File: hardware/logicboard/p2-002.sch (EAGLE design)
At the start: 18 parts, among them IC1 74LS07N, U1 DS18B20

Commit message: Writing.
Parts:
- removed H1, H2: STAND-OFF, SparkFun-Hardware:STAND-OFF
- removed JP2: RTC, SparkFun-Connectors:CONN_05
- added J0: (no value), con-jack:JACK-PLUG0
- added J1, J2: DIN5, SparkFun-Connectors:DIN5
- added SV1: (no value), con-ml:ML10LE
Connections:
- removed net V+: JP5.3
- net GND: now also J0.1, J0.2, J2.2; no longer JP2.2
- net MIRTN: now also J1.5
- net MISND: now also J1.4
- net MTRTN: now also J2.5
- net MTSND: now also J2.4
- net SCL: no longer JP2.4
- net SDA: no longer JP2.5
- net VCC: no longer JP2.1
- net VIN: now also J0.3, JP5.3

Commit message: Wiring.
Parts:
- removed C6, C7: 10n, resistor:C-EU025-024X044
- RN3: value 220 -> (none)
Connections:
- new net N$1: IC1B.O, RN3E.1
- new net N$2: IC1C.O, RN3G.1
- net GND: now also SV1-8.S; no longer C6.2, C7.2
- net GPIO1: now also SV1-1.S
- net GPIO2: now also SV1-7.S
- net MISO: now also SV1-3.S
- net MOSI: now also SV1-6.S
- net RX: now also IC1B.I, IC1C.I
- net SCK: now also SV1-5.S
- net VCC: now also RN3D.1, RN3F.1, SV1-4.S; no longer C6.1, C7.1
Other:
- moved on the sheet: D3, IC1A, IC1B, IC1C, OK1, RN3A, RN3B, RN3C, RN3E, RN3F, RN3G

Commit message: First working version of MIDI IN, MIDI THRU, SPI edition.
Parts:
- added JD1: DIN5, SparkFun-Connectors:DIN5
- added SV4: (no value), con-ml:ML14E
- added SV5: (no value), con-ml:ML10E
- J1: value DIN5 -> (none); device SparkFun-Connectors:DIN5 -> SparkFun-Connectors:CONN_05JST
- renumbered J2 to JD2, SV1 to SV3
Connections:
- net N$1 renamed MO
- net N$2 renamed MO2
- new net MO2RTN: RN3G.2, SV5-10.S
- new net MO2SND: RN3F.2, SV5-9.S
- new net MORTN: RN3E.2, SV5-8.S
- new net MOSND: RN3D.2, SV5-7.S
- net ANLG1: now also SV4-8.S
- net ANLG2: now also SV4-9.S
- net ANLG3: now also SV4-10.S
- net ANLG4: now also SV4-11.S
- net D7: now also J1.4
- net DTCT1: now also SV4-4.S
- net DTCT2: now also SV4-5.S
- net DTCT3: now also SV4-6.S
- net DTCT4: now also SV4-7.S
- net GATE: now also SV4-12.S
- net GND: now also J1.1, SV4-1.S, SV5-3.S, SV5-6.S
- net LED0: now also SV4-13.S
- net LED1: now also SV4-14.S
- net MIRTN: now also JD1.5, SV5-2.S; no longer J1.5
- net MISND: now also JD1.4, SV5-1.S; no longer J1.4
- net MTRTN: now also SV5-5.S
- net MTSND: now also SV5-4.S
- net RLY: now also SV4-3.S
- net RX: no longer IC1B.I, IC1C.I
- net SCL: now also J1.3
- net SDA: now also J1.2
- net TX: now also IC1B.I, IC1C.I
- net VCC: now also J1.5, SV4-2.S

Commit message: DIP SW.
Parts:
- added S1, S2: (no value), switch-dil:A1353HEX
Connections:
- net ANLG1: now also S2.1
- net ANLG2: now also S2.2
- net ANLG3: now also S2.4
- net ANLG4: now also S2.8
- net DTCT1: now also S1.1
- net DTCT2: now also S1.2
- net DTCT3: now also S1.4
- net DTCT4: now also S1.8
- net GND: now also S1.C, S2.C
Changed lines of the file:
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@@
 <part name="J1" library="SparkFun-Connectors" library_urn="urn:adsk.eagle:library:513" deviceset="CONN_05" device="JST" package3d_urn="urn:adsk.eagle:package:38120/1"/>
 <part name="SV5" library="con-ml" library_urn="urn:adsk.eagle:library:164" deviceset="ML10E" device="" package3d_urn="urn:adsk.eagle:package:8676/1"/>
+<part name="S1" library="switch-dil" library_urn="urn:adsk.eagle:library:375" deviceset="A1353HEX" device="" package3d_urn="urn:adsk.eagle:package:27207/1"/>
+<part name="S2" library="switch-dil" library_urn="urn:adsk.eagle:library:375" deviceset="A1353HEX" device="" package3d_urn="urn:adsk.eagle:package:27207/1"/>
 </parts>
 <sheets>
@@
 <attribute name="VALUE" x="68.834" y="83.439" size="1.778" layer="96" rot="MR0"/>
 </instance>
+<instance part="S1" gate="1" x="241.3" y="63.5" smashed="yes" rot="R270">
+<attribute name="NAME" x="236.22" y="67.945" size="1.778" layer="95"/>
+<attribute name="VALUE" x="236.22" y="54.61" size="1.778" layer="96"/>
+</instance>
+<instance part="S2" gate="1" x="241.3" y="48.26" smashed="yes" rot="R270">
+<attribute name="NAME" x="236.22" y="52.705" size="1.778" layer="95"/>
+<attribute name="VALUE" x="236.22" y="39.37" size="1.778" layer="96"/>
+</instance>
 </instances>
 <busses>
@@
 <label x="73.66" y="106.68" size="0.8128" layer="95" xref="yes"/>
 </segment>
+<segment>
+<pinref part="S1" gate="1" pin="C"/>
+<wire x1="233.68" y1="63.5" x2="231.14" y2="63.5" width="0.1524" layer="91"/>
+<label x="231.14" y="63.5" size="0.8128" layer="95" rot="R180" xref="yes"/>
+</segment>
+<segment>
+<pinref part="S2" gate="1" pin="C"/>
+<wire x1="233.68" y1="48.26" x2="231.14" y2="48.26" width="0.1524" layer="91"/>
+<label x="231.14" y="48.26" size="0.8128" layer="95" rot="R180" xref="yes"/>
+</segment>
 </net>
 <net name="VCC" class="2">
@@
 <label x="187.96" y="48.26" size="0.8128" layer="95" xref="yes"/>
 </segment>
+<segment>
+<pinref part="S2" gate="1" pin="8"/>
+<wire x1="248.92" y1="43.18" x2="251.46" y2="43.18" width="0.1524" layer="91"/>
+<label x="251.46" y="43.18" size="0.8128" layer="95" xref="yes"/>
+</segment>
 </net>
 <net name="ANLG3" class="0">
@@
 <label x="187.96" y="53.34" size="0.8128" layer="95" xref="yes"/>
 </segment>
+<segment>
+<pinref part="S2" gate="1" pin="4"/>
+<wire x1="248.92" y1="45.72" x2="251.46" y2="45.72" width="0.1524" layer="91"/>
+<label x="251.46" y="45.72" size="0.8128" layer="95" xref="yes"/>
+</segment>
 </net>
 <net name="ANLG2" class="0">
@@
 <label x="187.96" y="58.42" size="0.8128" layer="95" xref="yes"/>
 </segment>
+<segment>
+<pinref part="S2" gate="1" pin="2"/>
+<wire x1="248.92" y1="48.26" x2="251.46" y2="48.26" width="0.1524" layer="91"/>
+<label x="251.46" y="48.26" size="0.8128" layer="95" xref="yes"/>
+</segment>
 </net>
 <net name="ANLG1" class="0">
@@
 <wire x1="185.42" y1="63.5" x2="187.96" y2="63.5" width="0.1524" layer="91"/>
 <label x="187.96" y="63.5" size="0.8128" layer="95" xref="yes"/>
+</segment>
+<segment>
+<pinref part="S2" gate="1" pin="1"/>
+<wire x1="248.92" y1="50.8" x2="251.46" y2="50.8" width="0.1524" layer="91"/>
+<label x="251.46" y="50.8" size="0.8128" layer="95" xref="yes"/>
 </segment>
 </net>
@@
 <label x="152.4" y="48.26" size="0.8128" layer="95" xref="yes"/>
 </segment>
+<segment>
+<pinref part="S1" gate="1" pin="1"/>
+<wire x1="248.92" y1="66.04" x2="251.46" y2="66.04" width="0.1524" layer="91"/>
+<label x="251.46" y="66.04" size="0.8128" layer="95" xref="yes"/>
+</segment>
 </net>
 <net name="DTCT2" class="0">
@@
 <label x="152.4" y="43.18" size="0.8128" layer="95" xref="yes"/>
 </segment>
+<segment>
+<pinref part="S1" gate="1" pin="2"/>
+<wire x1="248.92" y1="63.5" x2="251.46" y2="63.5" width="0.1524" layer="91"/>
+<label x="251.46" y="63.5" size="0.8128" layer="95" xref="yes"/>
+</segment>
 </net>
 <net name="DTCT3" class="0">
@@
 <label x="152.4" y="38.1" size="0.8128" layer="95" xref="yes"/>
 </segment>
+<segment>
+<pinref part="S1" gate="1" pin="4"/>
+<wire x1="248.92" y1="60.96" x2="251.46" y2="60.96" width="0.1524" layer="91"/>
+<label x="251.46" y="60.96" size="0.8128" layer="95" xref="yes"/>
+</segment>
 </net>
 <net name="DTCT4" class="0">
@@
 <label x="152.4" y="33.02" size="0.8128" layer="95" xref="yes"/>
 </segment>
-</net>
+<segment>
+<pinref part="S1" gate="1" pin="8"/>
+<wire x1="248.92" y1="58.42" x2="251.46" y2="58.42" width="0.1524" layer="91"/>
+<label x="251.46" y="58.42" size="0.8128" layer="95" xref="yes"/>
+</segment>
+</net>

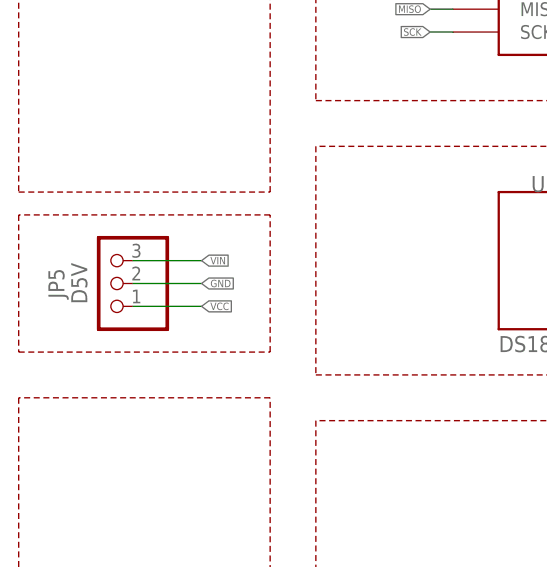
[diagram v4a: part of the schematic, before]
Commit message: Removed PWR pins.
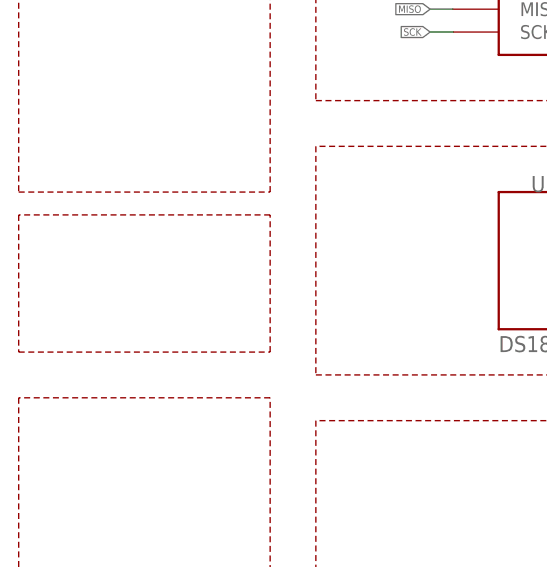
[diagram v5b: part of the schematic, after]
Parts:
- removed JP5: D5V, pinhead:PINHD-1X3
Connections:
- net GND: no longer JP5.2
- net VCC: no longer JP5.1
- net VIN: no longer JP5.3
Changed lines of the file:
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@@
 <part name="X10" library="wirepad" library_urn="urn:adsk.eagle:library:412" deviceset="PAD-N" device=""/>
 <part name="SUPPLY5" library="supply2" library_urn="urn:adsk.eagle:library:372" deviceset="VCC" device=""/>
-<part name="JP5" library="pinhead" library_urn="urn:adsk.eagle:library:325" deviceset="PINHD-1X3" device="" package3d_urn="urn:adsk.eagle:package:22458/2" value="D5V"/>
 <part name="JD1" library="SparkFun-Connectors" library_urn="urn:adsk.eagle:library:513" deviceset="DIN5" device="" package3d_urn="urn:adsk.eagle:package:38294/1"/>
 <part name="JD2" library="SparkFun-Connectors" library_urn="urn:adsk.eagle:library:513" deviceset="DIN5" device="" package3d_urn="urn:adsk.eagle:package:38294/1"/>
@@
 <attribute name="VALUE" x="231.14" y="226.06" size="1.778" layer="96" align="bottom-center"/>
 </instance>
-<instance part="JP5" gate="A" x="33.02" y="165.1" smashed="yes" rot="R180">
-<attribute name="NAME" x="27.94" y="165.1" size="1.778" layer="95" rot="R90" align="bottom-center"/>
-<attribute name="VALUE" x="30.48" y="165.1" size="1.778" layer="96" rot="R90" align="bottom-center"/>
-</instance>
 <instance part="JD1" gate="G$1" x="167.64" y="223.52" smashed="yes">
 <attribute name="NAME" x="167.64" y="217.932" size="1.778" layer="95" font="vector" align="bottom-center"/>
@@
 </segment>
 <segment>
-<pinref part="JP5" gate="A" pin="2"/>
-<wire x1="35.56" y1="165.1" x2="43.18" y2="165.1" width="0.1524" layer="91"/>
-<label x="43.18" y="165.1" size="0.8128" layer="95" xref="yes"/>
-</segment>
-<segment>
 <pinref part="JD2" gate="G$1" pin="2"/>
 <wire x1="167.64" y1="200.66" x2="167.64" y2="203.2" width="0.1524" layer="91"/>
@@
 </segment>
 <segment>
-<pinref part="JP5" gate="A" pin="1"/>
-<wire x1="35.56" y1="162.56" x2="43.18" y2="162.56" width="0.1524" layer="91"/>
-<label x="43.18" y="162.56" size="0.8128" layer="95" xref="yes"/>
-</segment>
-<segment>
 <pinref part="SV3" gate="-4" pin="S"/>
 <wire x1="312.42" y1="149.86" x2="309.88" y2="149.86" width="0.1524" layer="91"/>
@@
 </segment>
 <segment>
-<pinref part="JP5" gate="A" pin="3"/>
-<wire x1="35.56" y1="167.64" x2="43.18" y2="167.64" width="0.1524" layer="91"/>
-<label x="43.18" y="167.64" size="0.8128" layer="95" xref="yes"/>
-</segment>
-<segment>

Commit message: Clean up.
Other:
- moved on the sheet: C8, C9, D3, IC1A, IC1B, IC1C, IC1D, IC1E, IC1F, J0, J1, JD1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

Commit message: Stepper Driver v0.0.2-X.
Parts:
- removed J0: (no value), con-jack:JACK-PLUG0
- removed JD1, JD2: DIN5, SparkFun-Connectors:DIN5
- removed S1, S2: (no value), switch-dil:A1353HEX
- removed SV4: (no value), con-ml:ML14E
- removed SV5: (no value), con-ml:ML10E
- added C1: 22u, rcl:C-EU025-050X050
- added C10, C4, C5: 100n, rcl:C-EU025-024X044
- added C11, C12, C13: 10n, rcl:C-EUC2012
- added C2: 470n, rcl:C-EU050-024X044
- added C3: 1u, rcl:C-EU050-024X044
- added C6, C7: 10n, resistor:C-EU025-024X044
- added D1, D2: DIODE-1N4148, SparkFun-DiscreteSemi:DIODE-1N4148
- added F1: 1.8A, fuse:TE5
- added H1, H2: STAND-OFF, SparkFun-Hardware:STAND-OFF
- added IC11: 74LS153D, 74xx-us:74LS153D
- added IC12, IC13: LTC485S, linear-technology:LTC485S
- added IC2: 4066N, 40xx:4066N
- added IN, RX: (no value), wirepad:SMD2
- added J11, J12, J13, J14: Qwiic, SparkFun-Connectors:QWIIC_CONNECTORJS-1MM
- added J2: GPIO, SparkFun-Connectors:CONN_03JST-PTH
- added J3: Vcc, SparkFun-Connectors:CONN_02JST-PTH-2
- added J4: RLY, SparkFun-Connectors:CONN_02-JST-2MM-SMT
- added J5: SPI, SparkFun-Connectors:CONN_05JST-VERT
- added J6: LED, SparkFun-Connectors:CONN_03JST-PTH
- added JP1: PWRSEL, pinhead:PINHD-2X3
- added JP2: RTC, SparkFun-Connectors:CONN_05
- added JP3: MPXJMP, pinhead:PINHD-1X2
- added JP4: RLYJMP, pinhead:PINHD-1X2
- added JP5: D5V, pinhead:PINHD-1X3
- added JP6: LED, pinhead:PINHD-1X3
- added K1: G5V1, relay:G5V1
- added R1: 47k, resistor:R-EU_0204/5
- added R11: 10k, rcl:R-EU_M2012
- added R12, R13: 120, rcl:R-EU_M2012
- added R2, R5: 1k, resistor:R-EU_0204/5
- added R3, R4: 120, resistor:R-EU_0204/5
- added RN2: 10k, resistor-net:RN04
- added SV2: (no value), con-ml:ML20LE
- added T1: 2SC1815, transistor:2SC1815
- added V1: 5V, v-reg:78XXL
- J1: value (none) -> MKR
- RN3: value (none) -> 220
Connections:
- new net ANLG1R: IC2A.B
- new net ANLG2R: IC2B.B
- new net ANLG3R: IC2C.B
- new net ANLG4R: IC2D.B
- new net LED0A: J6.1, JP6.1, R4.1, SV2-5.S
- new net LED1A: J6.3, JP6.3, R3.1
- new net MIN: IC11A.1C1, IN.P, JP3.2, OK1.VO
- new net MRX: IC11A.1C0, IC12.RO
- new net MRX+: IC12.A, R12.1, SV2-9.S
- new net MRX-: IC12.B, R12.2, SV2-11.S
- new net MRXDTCT: IC11A.A, R11.1, SV2-10.S
- new net MTX+: IC13.A, R13.1, SV2-15.S
- new net MTX-: IC13.B, R13.2, SV2-16.S
- new net NC1: SV3-2.S
- new net NC2: SV3-9.S
- new net NC3: SV3-10.S
- new net RLYDRV: R1.2, R2.1, T1.B
- new net RLYOUT: J4.1, K12.S
- new net RLYSNK: D2.A, K11.2, T1.C
- new net V+: C1.1, C2.1, D1.C, JP1.1, JP5.3, SV2-2.S, V1.IN
- new net VCC/2: JP1.5, R5.2
- new net VOUT: F1.2, JP1.4, JP1.6
- new net VOUTRAW: C3.1, C4.1, D1.A, J4.2, JP4.2, K12.P, K12.P@1, V1.OUT
- new net VOUTRAW2: F1.1, JP4.1, K12.O
- net ANLG1: now also IC2A.A, RN2.2; no longer S2.1, SV4-8.S
- net ANLG2: now also IC2B.A, RN2.3; no longer S2.2, SV4-9.S
- net ANLG3: now also IC2C.A, RN2.4; no longer S2.4, SV4-10.S
- net ANLG4: now also IC2D.A, RN2.5; no longer S2.8, SV4-11.S
- net AREF: now also C5.1, R5.1
- net DTCT1: now also SV3-1.S; no longer S1.1, SV4-4.S
- net DTCT2: now also SV3-7.S; no longer S1.2, SV4-5.S
- net DTCT3: no longer S1.4, SV4-6.S
- net DTCT4: no longer S1.8, SV4-7.S
- net GATE: now also IC2A.C, IC2B.C, IC2C.C, IC2D.C; no longer SV4-12.S
- net GND: now also C1.2, C10.2, C11.2, C12.2, C13.2, C2.2, C3.2, C4.2, C5.2, C6.2, C7.2, IC11A.1C2, IC11A.1C3, IC11A.1G, IC11A.2C0, IC11A.2C1, IC11A.2C2, IC11A.2C3, IC11A.2G, IC11A.B, IC12.!RE, IC12.DE, IC12.DI, IC12.GND, IC13.GND, IC2P.VSS, J11.GND, J12.GND, J13.GND, J14.GND, J2.1, J3.1, J5.1, J6.2, JP2.2, JP5.1, JP6.2, R1.1, RN2.1, SV2-1.S, SV2-12.S, SV2-20.S, SV2-4.S, SV2-6.S, T1.E, V1.GND; no longer J0.1, J0.2, JD2.2, S1.C, S2.C, SV4-1.S, SV5-3.S, SV5-6.S
- net GPIO1: now also J2.2; no longer SV3-1.S
- net GPIO2: now also J2.3; no longer SV3-7.S
- net LED0: now also R4.2; no longer SV4-13.S
- net LED1: now also R3.2; no longer SV4-14.S
- net MIDIINSND: now also RN3B.1; no longer RN3A.1
- net MIRTN: now also SV2-8.S; no longer JD1.5, SV5-2.S
- net MISND: now also RN3B.2, SV2-7.S; no longer JD1.4, RN3A.2, SV5-1.S
- net MISO: now also J5.5
- net MO: now also RN3F.1; no longer RN3E.1
- net MO2: now also RN3H.1; no longer RN3G.1
- net MO2RTN: now also RN3H.2; no longer RN3G.2, SV5-10.S
- net MO2SND: now also RN3G.2; no longer RN3F.2, SV5-9.S
- net MORTN: now also RN3F.2, SV2-14.S; no longer RN3E.2, SV5-8.S
- net MOSI: now also J5.4
- net MOSND: now also RN3E.2, SV2-13.S; no longer RN3D.2, SV5-7.S
- net MT: now also RN3D.1; no longer RN3C.1
- net MTRTN: now also RN3D.2, SV2-18.S; no longer JD2.5, RN3C.2, SV5-5.S
- net MTSND: now also RN3C.2, SV2-17.S; no longer JD2.4, RN3B.2, SV5-4.S
- net RLY: now also R2.2; no longer SV4-3.S
- net RST: now also SV2-3.S
- net RX: now also IC11A.1Y, JP3.1, RX.P; no longer OK1.VO
- net SCK: now also J5.3
- net SCL: now also J11.SCL, J12.SCL, J13.SCL, J14.SCL, JP2.4
- net SDA: now also J11.SDA, J12.SDA, J13.SDA, J14.SDA, JP2.5
- net TX: now also IC13.DI
- net VCC: now also C10.1, C11.1, C12.1, C13.1, C6.1, C7.1, D2.C, IC12.VCC, IC13.!RE, IC13.DE, IC13.VCC, IC2P.VDD, J11.VCC, J12.VCC, J13.VCC, J14.VCC, J3.2, J5.2, JP1.3, JP2.1, JP5.2, K11.1, R11.2, RN3C.1, RN3E.1, RN3G.1, SV2-19.S; no longer RN3B.1, RN3D.1, RN3F.1, SV4-2.S
- net VIN: now also JP1.2; no longer J0.3
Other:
- moved on the sheet: C8, C9, D3, IC1A, IC1B, IC1C, IC1D, IC1E, IC1F, J1, OK1, RN1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
